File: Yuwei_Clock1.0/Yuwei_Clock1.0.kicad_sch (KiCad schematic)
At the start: 4 parts

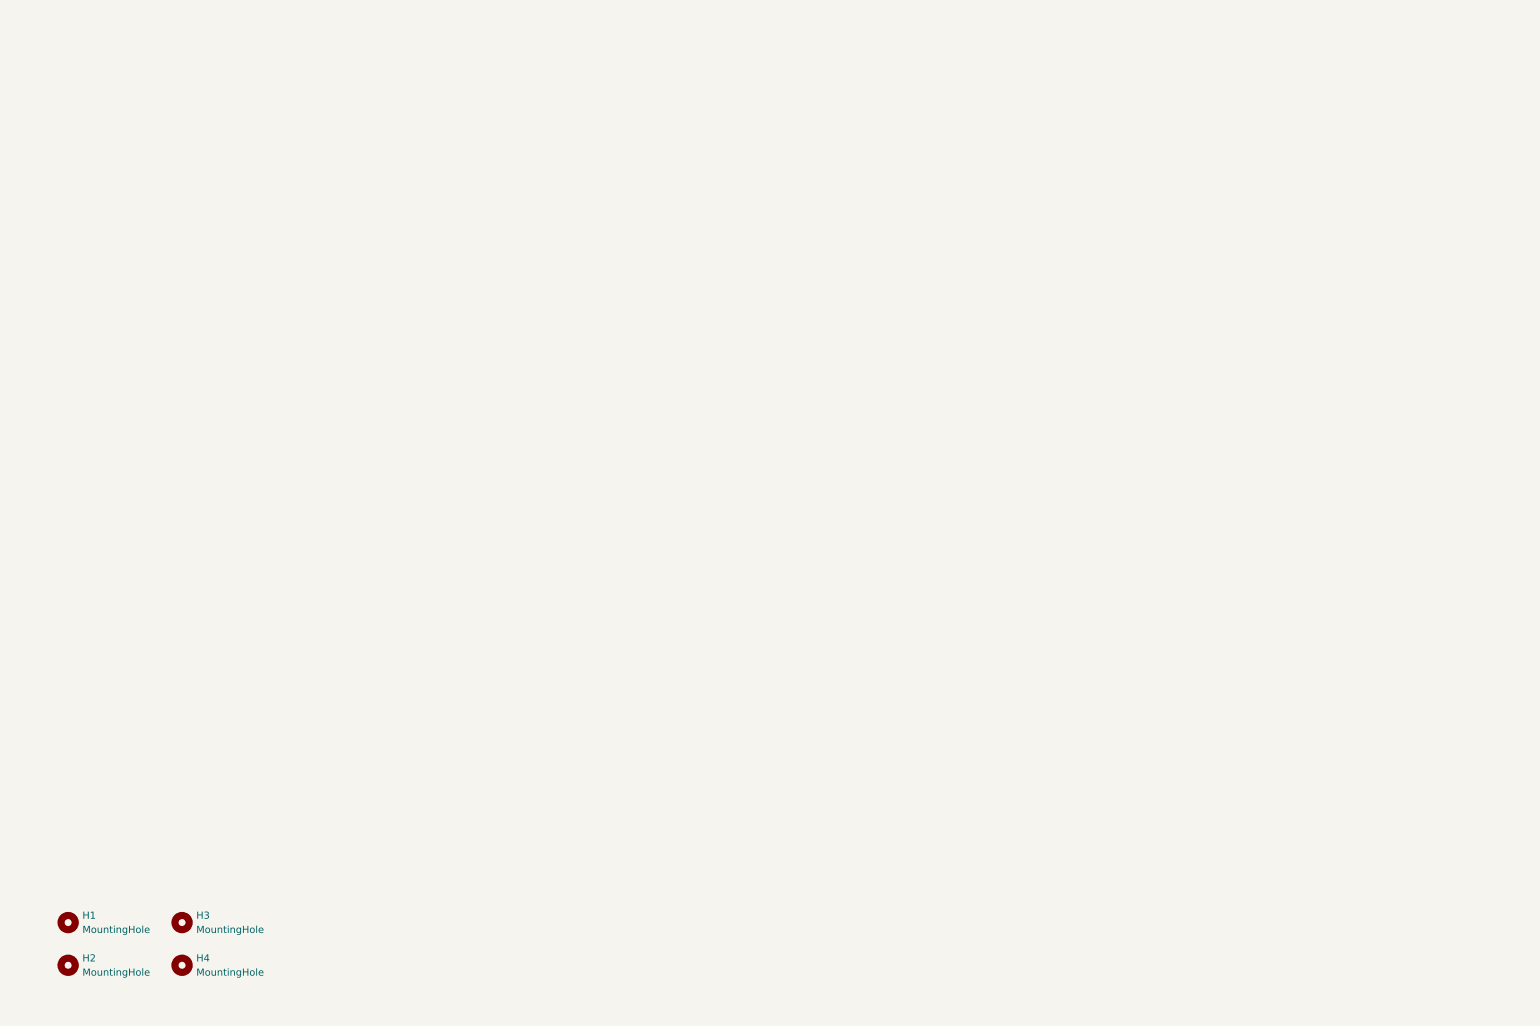
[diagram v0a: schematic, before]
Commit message: New schematic of week 1
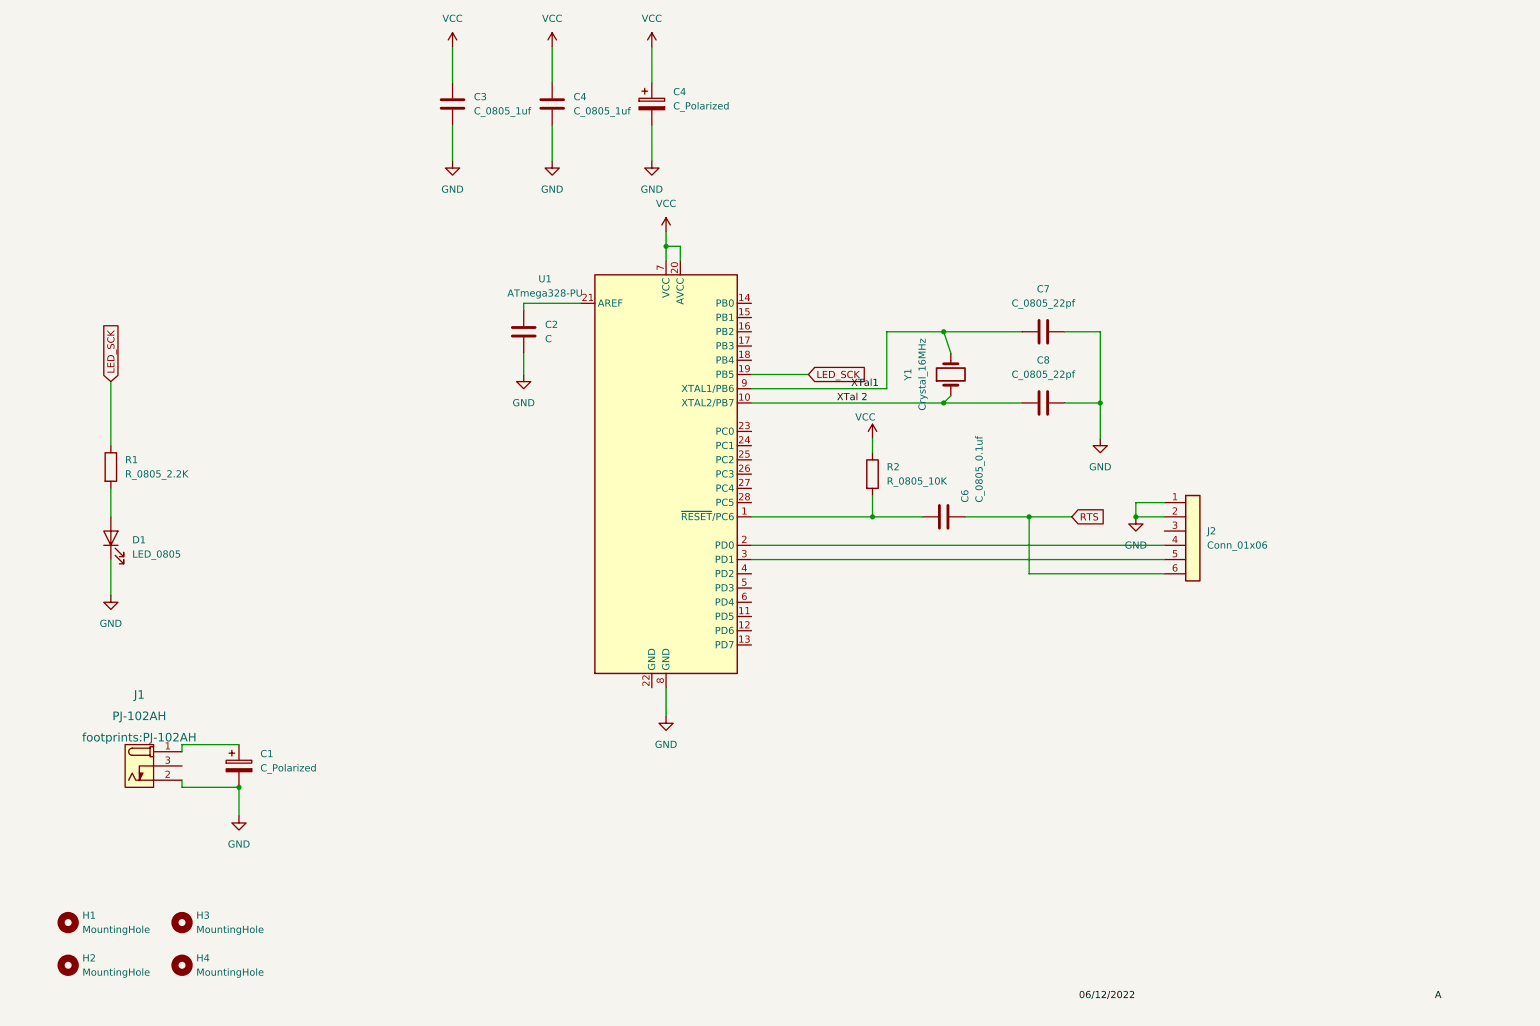
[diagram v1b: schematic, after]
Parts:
- added C1, C4: C_Polarized, symbol DEVICE:C_Polarized
- added C2: C, symbol DEVICE:C
- added C3, C4: C_0805_1uf, footprints:C_0805_2012Metric, symbol HPS:C_0805_1uf
- added C6: C_0805_0.1uf, footprints:C_0805_2012Metric, symbol HPS:C_0805_0.1uf
- added C7, C8: C_0805_22pf, footprints:C_0805_2012Metric, symbol HPS:C_0805_22pf
- added D1: LED_0805, footprints:LED_0805_2012Metric, symbol HPS:LED_0805
- added J1: PJ-102AH, footprints:PJ-102AH, symbol HPS:PJ-102AH
- added J2: Conn_01x06, footprints:PinHeader_1x06_P2.54mm_Vertical, symbol HPS:Conn_01x06
- added R1: R_0805_2.2K, footprints:R_0805_2012Metric, symbol HPS:R_0805_2.2K
- added R2: R_0805_10K, footprints:R_0805_2012Metric, symbol HPS:R_0805_10K
- added U1: ATmega328-PU, footprints:DIP-28_W7.62mm, symbol HPS:ATmega328-PU
- added Y1: Crystal_16MHz, footprints:Crystal_SMD_HC49-SD, symbol HPS:Crystal_16MHz
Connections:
- new net: C1.1, J1.1 (POLE)
- new net: D1.2 (A), R1.2
- new net: C6.1, R2.2, U1.1 (~{RESET}/PC6)
- new net: J2.4 (Pin_4), U1.2 (PD0)
- new net: C2.1, U1.21 (AREF)
- new net: J2.5 (Pin_5), U1.3 (PD1)
- new net GND: C1.2, C2.2, C3.2, C4.2, C4.2, C7.2, C8.2, D1.1 (K), J1.2 (OUT), J2.1 (Pin_1), J2.2 (Pin_2), U1.8 (GND)
- new net LED_SCK: R1.1, U1.19 (PB5)
- new net RTS: C6.2, J2.6 (Pin_6)
- new net VCC: C3.1, C4.1, C4.1, R2.1, U1.20 (AVCC), U1.7 (VCC)
- new net XTal 2: C8.1, U1.10 (XTAL2/PB7), Y1.1
- new net XTal1: C7.1, U1.9 (XTAL1/PB6), Y1.2

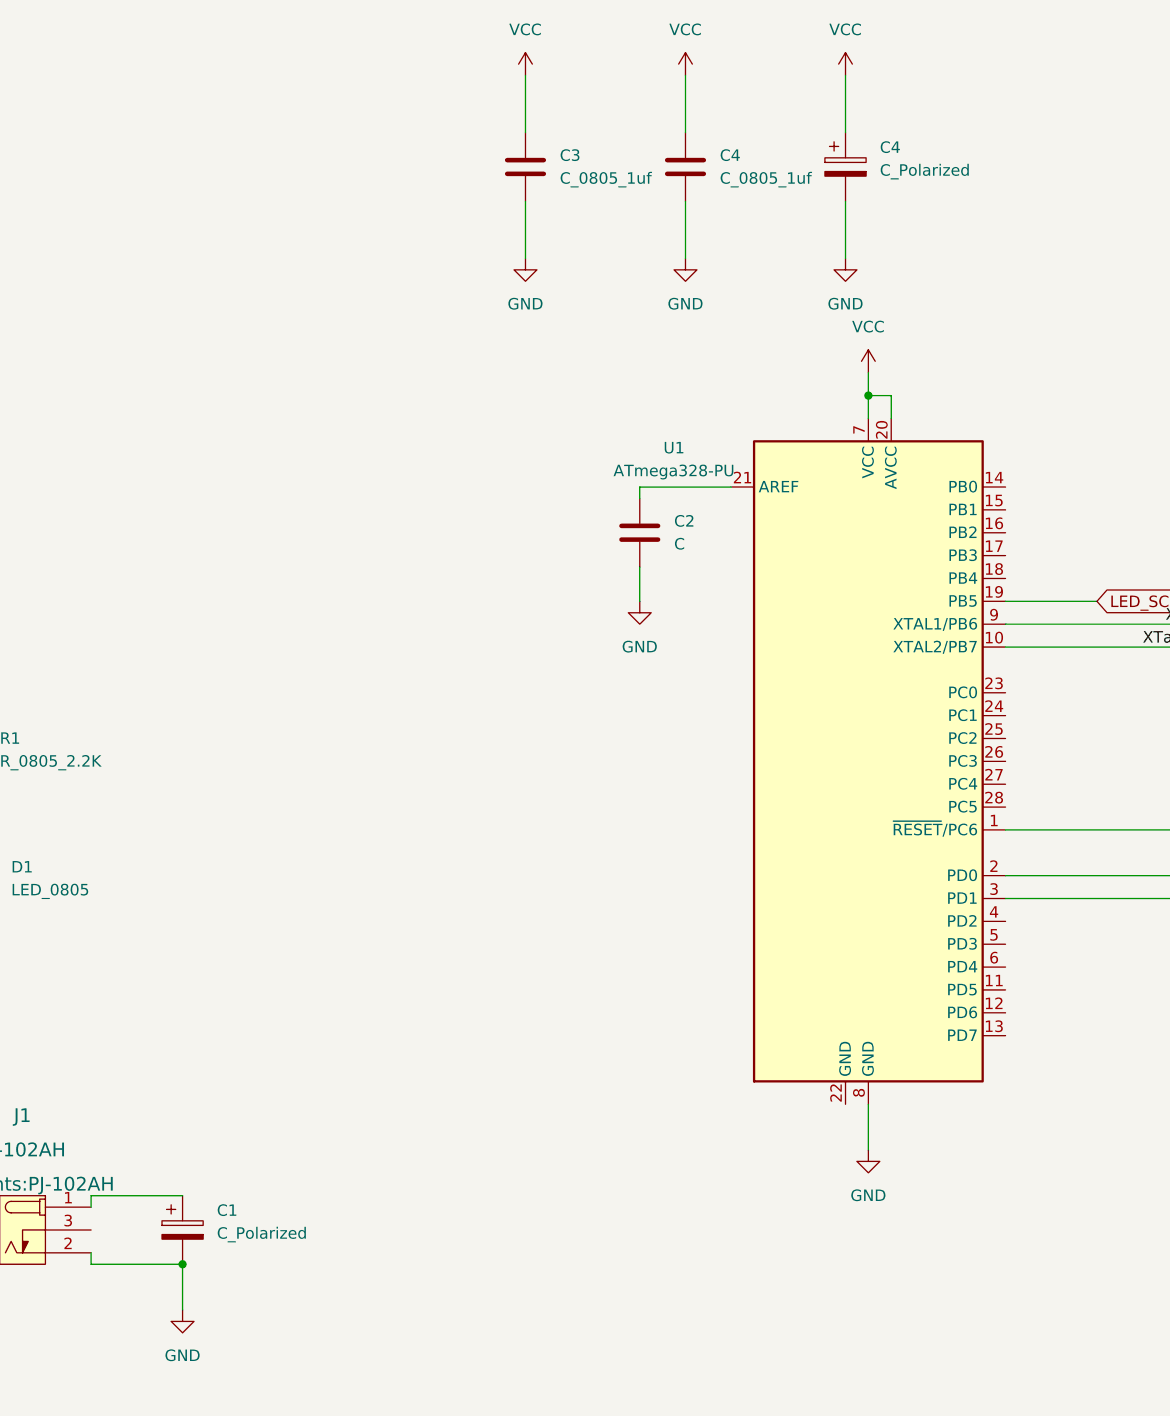
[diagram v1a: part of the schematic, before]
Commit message: Change polar capacitor to C_0805_10uf
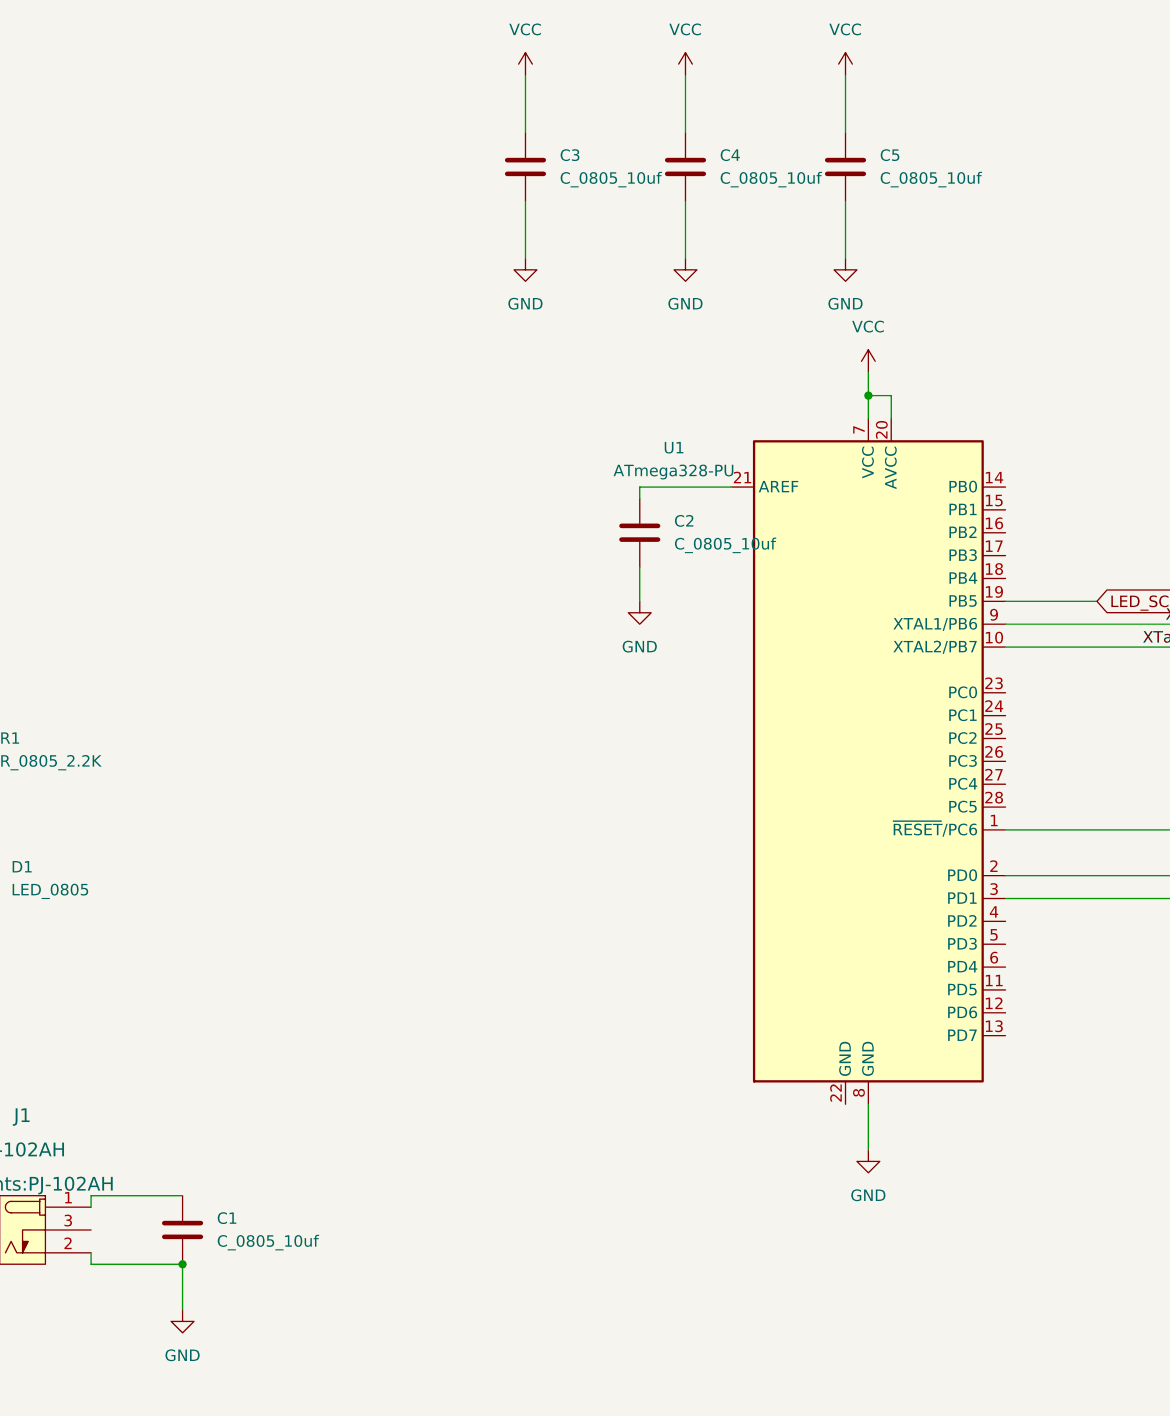
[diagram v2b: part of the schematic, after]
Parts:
- removed C1, C4: C_Polarized, symbol DEVICE:C_Polarized
- removed C2: C, symbol DEVICE:C
- removed C3, C4: C_0805_1uf, footprints:C_0805_2012Metric, symbol HPS:C_0805_1uf
- added C1, C2, C3, C4, C5: C_0805_10uf, footprints:C_0805_2012Metric, symbol HPS:C_0805_10uf
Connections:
- net GND: now also C1.2, C2.2, C3.2, C4.2, C5.2
- net VCC: now also C3.1, C4.1, C5.1
- net at J1.1 (POLE): now also C1.1
- net at U1.21 (AREF): now also C2.1

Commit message: Update with Schematic and PCB
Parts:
- removed C1, C3, C4, C5: C_0805_10uf, footprints:C_0805_2012Metric, symbol HPS:C_0805_10uf
- removed C6: C_0805_0.1uf, footprints:C_0805_2012Metric, symbol HPS:C_0805_0.1uf
- removed J2: Conn_01x06, footprints:PinHeader_1x06_P2.54mm_Vertical, symbol HPS:Conn_01x06
- added C2, C3: C_0805_0.1uf, footprints:C_0805_2012Metric, symbol HPS:C_0805_0.1uf
- added C6, C7: C_0805_1uf, footprints:C_0805_2012Metric, symbol HPS:C_0805_1uf
- added J?: Conn_01x06, footprints:PinHeader_1x06_P2.54mm_Vertical, symbol HPS:Conn_01x06
- added R3, R4: R_0805_47, footprints:R_0805_2012Metric, symbol HPS:R_0805_47
- added SW1: Omron_B3F_SPST, footprints:SW_SPST_Omron_B3FS-100xP, symbol HPS:Omron_B3F_SPST
- added U2: L7805, footprints:TO-220-3_Horizontal_TabDown, symbol HPS:L7805
- renumbered C2 to C1, C7 to C4, C8 to C5, J1 to J2
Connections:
- net GND: now also U1.22 (GND), C2.2, C6.2, C7.2, J?.1 (Pin_1), J?.2 (Pin_2), SW1.1 (A), SW1.2 (A), U2.2 (GND)
- net VCC: now also C2.1, C7.1, U2.3 (OUT)
- net at J2.1 (POLE): now also C6.1, U2.1 (IN)
- net RESET: now reaches R2.2, U1.1 (~{RESET}/PC6)
- net RESET: now also C3.1, SW1.3 (B), SW1.4 (B)
- net RXD: now reaches U1.2 (PD0)
- net RXD: now also R4.2
- net TXD: now reaches U1.4 (PD2)
- net TXD: now also R3.1
- net XTal 2: no longer names the net of C5.1, U1.10 (XTAL2/PB7)
- net XTal 2: now also Y1.2; no longer Y1.1
- net XTal1: no longer names the net of C4.1, U1.9 (XTAL1/PB6)
- net XTal1: now also Y1.1; no longer Y1.2
- new net: J?.4 (Pin_4), R3.2
- new net: J?.5 (Pin_5), R4.1
- new net: C3.2, J?.6 (Pin_6)
- no-connect marks 0 -> 2
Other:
- note added: "LED"
- note added: "MCU"
- note added: "Power Input"
- note added: "Serial"
- note added: "Vf = 2v Vr = 3v 10mcd @ 1.35mA therefore R = 2.2K0hm"
- moved on the sheet: C1, C4, C5, D1, J2, R1, U1

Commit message: Update with RTC
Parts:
- added BZ1: Buzzer, footprints:Buzzer_TDK_PS1240P02BT_D12.2mm_H6.5mm, symbol HPS:Buzzer
- added DS1: LED_Display_1001, footprints:Adafruit-1001-0-0-MFG, symbol HPS:LED_Display_1001
- added R5: R_0805_1K, footprints:R_0805_2012Metric, symbol HPS:R_0805_1K
- added R6: PhotoconductivePhotocell, footprints:R_LDR_4.9x4.2mm_P2.54mm_Vertical, symbol HPS:PhotoconductivePhotocell
- gave numbers to parts that had none: 1
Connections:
- net GND: now also BZ1.2 (+), R6.2
- net LED_SCK: now also U1.17 (PB3)
- net at U1.14 (PB0): now also R6.1
- net at U1.24 (PC1): now also R5.2
- new net: BZ1.1 (-), R5.1
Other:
- note added: "7_Segment Display"
- note added: "Still need Joystick Module and SG90 servo"
- moved on the sheet: C1, C2, C4, C5, C6, C7, D1, J2, R1, R2, U1, U2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
